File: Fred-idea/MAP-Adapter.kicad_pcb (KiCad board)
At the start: 2 copper layers, 19.8 x 11.5 mm, 2 parts, among them U1 SOP8, U6 SSOP8

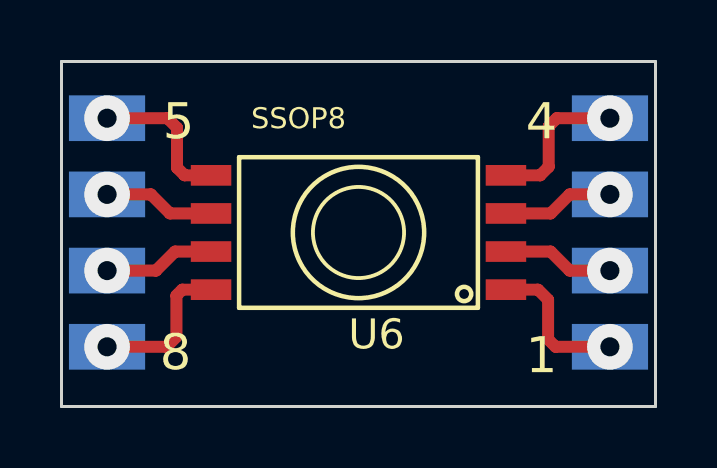
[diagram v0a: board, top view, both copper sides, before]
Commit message: Widened traces on top (SSOP) layer to the same width as the SSOP pads.
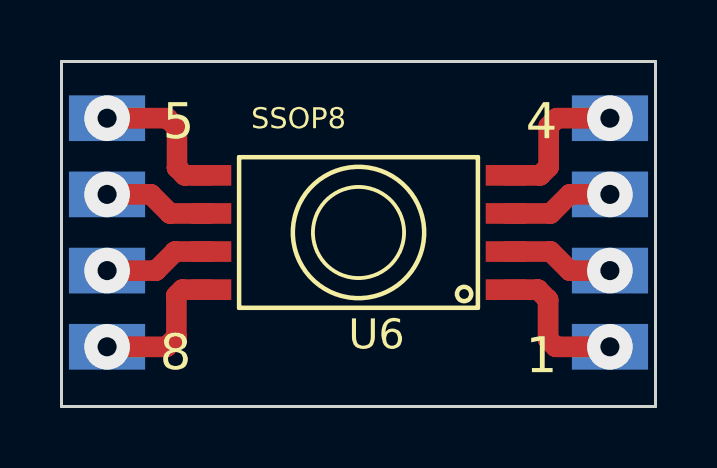
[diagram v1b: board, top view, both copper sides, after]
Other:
- net class SSOP: trace_width 0.4 -> 0.69
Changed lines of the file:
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@@
   (net_class SSOP ""
     (clearance 0.254)
-    (trace_width 0.4)
+    (trace_width 0.69)
     (via_dia 1.524)
     (via_drill 1.2)
@@
   (gr_line (start 226.3 144.8) (end 206.5 144.8) (angle 90) (layer Edge.Cuts) (width 0.1))
   (gr_line (start 226.3 156.3) (end 226.3 144.8) (angle 90) (layer Edge.Cuts) (width 0.1))
-  (segment (start 221.315 151.135) (end 222.805 151.135) (width 0.4) (layer F.Cu) (net 1))
-  (segment (start 224.78 151.77) (end 224.782 151.77) (width 0.4) (layer B.Cu) (net 1))
+  (segment (start 221.315 151.135) (end 222.805 151.135) (width 0.69) (layer F.Cu) (net 1))
+  (segment (start 222.805 151.135) (end 223.44 151.77) (width 0.69) (layer F.Cu) (net 1))
+  (segment (start 223.44 151.77) (end 224.78 151.77) (width 0.69) (layer F.Cu) (net 1))
   (via (at 224.78 151.77) (size 1.524) (layers F.Cu B.Cu) (net 1))
-  (segment (start 223.44 151.77) (end 224.78 151.77) (width 0.4) (layer F.Cu) (net 1))
-  (segment (start 222.805 151.135) (end 223.44 151.77) (width 0.4) (layer F.Cu) (net 1))
-  (segment (start 221.315 149.865) (end 222.805 149.865) (width 0.4) (layer F.Cu) (net 2))
-  (segment (start 224.78 149.23) (end 224.782 149.23) (width 0.4) (layer B.Cu) (net 2))
+  (segment (start 224.78 151.77) (end 224.782 151.77) (width 0.69) (layer B.Cu) (net 1))
+  (segment (start 221.315 149.865) (end 222.805 149.865) (width 0.69) (layer F.Cu) (net 2))
+  (segment (start 222.805 149.865) (end 223.44 149.23) (width 0.69) (layer F.Cu) (net 2))
+  (segment (start 223.44 149.23) (end 224.78 149.23) (width 0.69) (layer F.Cu) (net 2))
   (via (at 224.78 149.23) (size 1.524) (layers F.Cu B.Cu) (net 2))
-  (segment (start 223.44 149.23) (end 224.78 149.23) (width 0.4) (layer F.Cu) (net 2))
-  (segment (start 222.805 149.865) (end 223.44 149.23) (width 0.4) (layer F.Cu) (net 2))
-  (segment (start 221.315 148.595) (end 222.455 148.595) (width 0.4) (layer F.Cu) (net 3))
-  (segment (start 224.78 146.69) (end 224.782 146.69) (width 0.4) (layer B.Cu) (net 3))
+  (segment (start 224.78 149.23) (end 224.782 149.23) (width 0.69) (layer B.Cu) (net 2))
+  (segment (start 221.315 148.595) (end 222.455 148.595) (width 0.69) (layer F.Cu) (net 3))
+  (segment (start 222.455 148.595) (end 222.74 148.31) (width 0.69) (layer F.Cu) (net 3))
+  (segment (start 222.74 148.31) (end 222.74 146.96) (width 0.69) (layer F.Cu) (net 3))
+  (segment (start 222.74 146.96) (end 223.01 146.69) (width 0.69) (layer F.Cu) (net 3))
+  (segment (start 223.01 146.69) (end 224.78 146.69) (width 0.69) (layer F.Cu) (net 3))
   (via (at 224.78 146.69) (size 1.524) (layers F.Cu B.Cu) (net 3))
-  (segment (start 223.01 146.69) (end 224.78 146.69) (width 0.4) (layer F.Cu) (net 3))
-  (segment (start 222.74 146.96) (end 223.01 146.69) (width 0.4) (layer F.Cu) (net 3))
-  (segment (start 222.74 148.31) (end 222.74 146.96) (width 0.4) (layer F.Cu) (net 3))
-  (segment (start 222.455 148.595) (end 222.74 148.31) (width 0.4) (layer F.Cu) (net 3))
-  (segment (start 221.315 152.405) (end 222.385 152.405) (width 0.4) (layer F.Cu) (net 4))
-  (segment (start 224.78 154.31) (end 224.782 154.31) (width 0.4) (layer B.Cu) (net 4))
+  (segment (start 224.78 146.69) (end 224.782 146.69) (width 0.69) (layer B.Cu) (net 3))
+  (segment (start 221.315 152.405) (end 222.385 152.405) (width 0.69) (layer F.Cu) (net 4))
+  (segment (start 222.385 152.405) (end 222.72 152.74) (width 0.69) (layer F.Cu) (net 4))
+  (segment (start 222.72 152.74) (end 222.72 154.06) (width 0.69) (layer F.Cu) (net 4))
+  (segment (start 222.72 154.06) (end 222.97 154.31) (width 0.69) (layer F.Cu) (net 4))
+  (segment (start 222.97 154.31) (end 224.78 154.31) (width 0.69) (layer F.Cu) (net 4))
   (via (at 224.78 154.31) (size 1.524) (layers F.Cu B.Cu) (net 4))
-  (segment (start 222.97 154.31) (end 224.78 154.31) (width 0.4) (layer F.Cu) (net 4))
-  (segment (start 222.72 154.06) (end 222.97 154.31) (width 0.4) (layer F.Cu) (net 4))
-  (segment (start 222.72 152.74) (end 222.72 154.06) (width 0.4) (layer F.Cu) (net 4))
-  (segment (start 222.385 152.405) (end 222.72 152.74) (width 0.4) (layer F.Cu) (net 4))
-  (segment (start 211.485 148.595) (end 210.605 148.595) (width 0.4) (layer F.Cu) (net 5))
-  (segment (start 208.02 146.69) (end 208.018 146.69) (width 0.4) (layer B.Cu) (net 5))
+  (segment (start 224.78 154.31) (end 224.782 154.31) (width 0.69) (layer B.Cu) (net 4))
+  (segment (start 211.485 148.595) (end 210.605 148.595) (width 0.69) (layer F.Cu) (net 5))
+  (segment (start 210.605 148.595) (end 210.35 148.34) (width 0.69) (layer F.Cu) (net 5))
+  (segment (start 210.35 148.34) (end 210.35 147.01) (width 0.69) (layer F.Cu) (net 5))
+  (segment (start 210.35 147.01) (end 210.03 146.69) (width 0.69) (layer F.Cu) (net 5))
+  (segment (start 210.03 146.69) (end 208.02 146.69) (width 0.69) (layer F.Cu) (net 5))
   (via (at 208.02 146.69) (size 1.524) (layers F.Cu B.Cu) (net 5))
-  (segment (start 210.03 146.69) (end 208.02 146.69) (width 0.4) (layer F.Cu) (net 5))
-  (segment (start 210.35 147.01) (end 210.03 146.69) (width 0.4) (layer F.Cu) (net 5))
-  (segment (start 210.35 148.34) (end 210.35 147.01) (width 0.4) (layer F.Cu) (net 5))
-  (segment (start 210.605 148.595) (end 210.35 148.34) (width 0.4) (layer F.Cu) (net 5))
-  (segment (start 211.485 149.865) (end 210.115 149.865) (width 0.4) (layer F.Cu) (net 6))
-  (segment (start 208.02 149.23) (end 208.018 149.23) (width 0.4) (layer B.Cu) (net 6))
+  (segment (start 208.02 146.69) (end 208.018 146.69) (width 0.69) (layer B.Cu) (net 5))
+  (segment (start 211.485 149.865) (end 210.115 149.865) (width 0.69) (layer F.Cu) (net 6))
+  (segment (start 210.115 149.865) (end 209.48 149.23) (width 0.69) (layer F.Cu) (net 6))
+  (segment (start 209.48 149.23) (end 208.02 149.23) (width 0.69) (layer F.Cu) (net 6))
   (via (at 208.02 149.23) (size 1.524) (layers F.Cu B.Cu) (net 6))
-  (segment (start 209.48 149.23) (end 208.02 149.23) (width 0.4) (layer F.Cu) (net 6))
-  (segment (start 210.115 149.865) (end 209.48 149.23) (width 0.4) (layer F.Cu) (net 6))
-  (segment (start 211.485 151.135) (end 210.285 151.135) (width 0.4) (layer F.Cu) (net 7))
-  (segment (start 208.02 151.77) (end 208.018 151.77) (width 0.4) (layer B.Cu) (net 7))
+  (segment (start 208.02 149.23) (end 208.018 149.23) (width 0.69) (layer B.Cu) (net 6))
+  (segment (start 211.485 151.135) (end 210.285 151.135) (width 0.69) (layer F.Cu) (net 7))
+  (segment (start 210.285 151.135) (end 209.65 151.77) (width 0.69) (layer F.Cu) (net 7))
+  (segment (start 209.65 151.77) (end 208.02 151.77) (width 0.69) (layer F.Cu) (net 7))
   (via (at 208.02 151.77) (size 1.524) (layers F.Cu B.Cu) (net 7))
-  (segment (start 209.65 151.77) (end 208.02 151.77) (width 0.4) (layer F.Cu) (net 7))
-  (segment (start 210.285 151.135) (end 209.65 151.77) (width 0.4) (layer F.Cu) (net 7))
-  (segment (start 211.485 152.405) (end 210.525 152.405) (width 0.4) (layer F.Cu) (net 8))
-  (segment (start 208.02 154.31) (end 208.018 154.31) (width 0.4) (layer B.Cu) (net 8))
+  (segment (start 208.02 151.77) (end 208.018 151.77) (width 0.69) (layer B.Cu) (net 7))
+  (segment (start 211.485 152.405) (end 210.525 152.405) (width 0.69) (layer F.Cu) (net 8))
+  (segment (start 210.525 152.405) (end 210.33 152.6) (width 0.69) (layer F.Cu) (net 8))
+  (segment (start 210.33 152.6) (end 210.33 153.98) (width 0.69) (layer F.Cu) (net 8))
+  (segment (start 210.33 153.98) (end 210 154.31) (width 0.69) (layer F.Cu) (net 8))
+  (segment (start 210 154.31) (end 208.02 154.31) (width 0.69) (layer F.Cu) (net 8))
   (via (at 208.02 154.31) (size 1.524) (layers F.Cu B.Cu) (net 8))
-  (segment (start 210 154.31) (end 208.02 154.31) (width 0.4) (layer F.Cu) (net 8))
-  (segment (start 210.33 153.98) (end 210 154.31) (width 0.4) (layer F.Cu) (net 8))
-  (segment (start 210.33 152.6) (end 210.33 153.98) (width 0.4) (layer F.Cu) (net 8))
-  (segment (start 210.525 152.405) (end 210.33 152.6) (width 0.4) (layer F.Cu) (net 8))
+  (segment (start 208.02 154.31) (end 208.018 154.31) (width 0.69) (layer B.Cu) (net 8))
 )

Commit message: Edges of PCB are now at the edge of the solder mask.
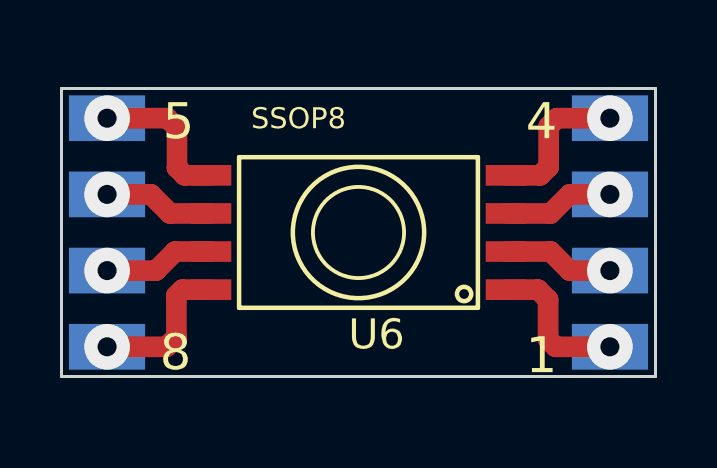
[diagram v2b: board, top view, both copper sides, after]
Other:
- board size 19.8 x 11.5 mm -> 19.8 x 9.6 mm
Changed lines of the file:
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@@
     )
   )
+  (dimension 9.6 (width 0.3) (layer Eco1.User)
+    (gr_text "0.3780 in" (at 230.95 150.5 90) (layer Eco1.User)
+      (effects (font (size 1.5 1.5) (thickness 0.3)))
+    )
+    (feature1 (pts (xy 226.6 145.7) (xy 232.3 145.7)))
+    (feature2 (pts (xy 226.6 155.3) (xy 232.3 155.3)))
+    (crossbar (pts (xy 229.6 155.3) (xy 229.6 145.7)))
+    (arrow1a (pts (xy 229.6 145.7) (xy 230.18642 146.826503)))
+    (arrow1b (pts (xy 229.6 145.7) (xy 229.01358 146.826503)))
+    (arrow2a (pts (xy 229.6 155.3) (xy 230.18642 154.173497)))
+    (arrow2b (pts (xy 229.6 155.3) (xy 229.01358 154.173497)))
+  )
+  (dimension 19.8 (width 0.3) (layer Eco1.User)
+    (gr_text "0.7795 in" (at 216.4 142.950001) (layer Eco1.User)
+      (effects (font (size 1.5 1.5) (thickness 0.3)))
+    )
+    (feature1 (pts (xy 226.3 145.4) (xy 226.3 141.600001)))
+    (feature2 (pts (xy 206.5 145.4) (xy 206.5 141.600001)))
+    (crossbar (pts (xy 206.5 144.300001) (xy 226.3 144.300001)))
+    (arrow1a (pts (xy 226.3 144.300001) (xy 225.173497 144.886421)))
+    (arrow1b (pts (xy 226.3 144.300001) (xy 225.173497 143.713581)))
+    (arrow2a (pts (xy 206.5 144.300001) (xy 207.626503 144.886421)))
+    (arrow2b (pts (xy 206.5 144.300001) (xy 207.626503 143.713581)))
+  )
+  (dimension 9.6 (width 0.3) (layer Dwgs.User)
+    (gr_text "9.600 mm" (at 203.55 150.5 90) (layer Dwgs.User)
+      (effects (font (size 1.5 1.5) (thickness 0.3)))
+    )
+    (feature1 (pts (xy 206.2 145.7) (xy 202.2 145.7)))
+    (feature2 (pts (xy 206.2 155.3) (xy 202.2 155.3)))
+    (crossbar (pts (xy 204.9 155.3) (xy 204.9 145.7)))
+    (arrow1a (pts (xy 204.9 145.7) (xy 205.48642 146.826503)))
+    (arrow1b (pts (xy 204.9 145.7) (xy 204.31358 146.826503)))
+    (arrow2a (pts (xy 204.9 155.3) (xy 205.48642 154.173497)))
+    (arrow2b (pts (xy 204.9 155.3) (xy 204.31358 154.173497)))
+  )
+  (dimension 19.8 (width 0.3) (layer Dwgs.User)
+    (gr_text "19.800 mm" (at 216.4 158.349999) (layer Dwgs.User)
+      (effects (font (size 1.5 1.5) (thickness 0.3)))
+    )
+    (feature1 (pts (xy 226.3 155.6) (xy 226.3 159.699999)))
+    (feature2 (pts (xy 206.5 155.6) (xy 206.5 159.699999)))
+    (crossbar (pts (xy 206.5 156.999999) (xy 226.3 156.999999)))
+    (arrow1a (pts (xy 226.3 156.999999) (xy 225.173497 157.586419)))
+    (arrow1b (pts (xy 226.3 156.999999) (xy 225.173497 156.413579)))
+    (arrow2a (pts (xy 206.5 156.999999) (xy 207.626503 157.586419)))
+    (arrow2b (pts (xy 206.5 156.999999) (xy 207.626503 156.413579)))
+  )
+  (gr_line (start 206.5 155.3) (end 206.5 145.7) (angle 90) (layer Edge.Cuts) (width 0.1))
+  (gr_line (start 226.3 155.3) (end 206.5 155.3) (angle 90) (layer Edge.Cuts) (width 0.1))
+  (gr_line (start 226.3 145.7) (end 226.3 155.3) (angle 90) (layer Edge.Cuts) (width 0.1))
+  (gr_line (start 206.5 145.7) (end 226.3 145.7) (angle 90) (layer Edge.Cuts) (width 0.1))
   (gr_text 8 (at 210.3 154.5) (layer F.SilkS)
     (effects (font (size 1.2 1.2) (thickness 0.18)))
@@
     (effects (font (size 1.2 1.2) (thickness 0.18)))
   )
-  (dimension 19.8 (width 0.3) (layer Dwgs.User)
-    (gr_text "19.800 mm" (at 216.4 159.249999) (layer Dwgs.User)
-      (effects (font (size 1.5 1.5) (thickness 0.3)))
-    )
-    (feature1 (pts (xy 226.3 156.6) (xy 226.3 160.599999)))
-    (feature2 (pts (xy 206.5 156.6) (xy 206.5 160.599999)))
-    (crossbar (pts (xy 206.5 157.899999) (xy 226.3 157.899999)))
-    (arrow1a (pts (xy 226.3 157.899999) (xy 225.173497 158.486419)))
-    (arrow1b (pts (xy 226.3 157.899999) (xy 225.173497 157.313579)))
-    (arrow2a (pts (xy 206.5 157.899999) (xy 207.626503 158.486419)))
-    (arrow2b (pts (xy 206.5 157.899999) (xy 207.626503 157.313579)))
-  )
-  (dimension 11.5 (width 0.3) (layer Dwgs.User)
-    (gr_text "11.500 mm" (at 203.75 150.55 90) (layer Dwgs.User)
-      (effects (font (size 1.5 1.5) (thickness 0.3)))
-    )
-    (feature1 (pts (xy 206.3 144.8) (xy 202.4 144.8)))
-    (feature2 (pts (xy 206.3 156.3) (xy 202.4 156.3)))
-    (crossbar (pts (xy 205.1 156.3) (xy 205.1 144.8)))
-    (arrow1a (pts (xy 205.1 144.8) (xy 205.68642 145.926503)))
-    (arrow1b (pts (xy 205.1 144.8) (xy 204.51358 145.926503)))
-    (arrow2a (pts (xy 205.1 156.3) (xy 205.68642 155.173497)))
-    (arrow2b (pts (xy 205.1 156.3) (xy 204.51358 155.173497)))
-  )
-  (dimension 11.5 (width 0.3) (layer Eco1.User)
-    (gr_text "0.4528 in" (at 229.15 150.55 90) (layer Eco1.User)
-      (effects (font (size 1.5 1.5) (thickness 0.3)))
-    )
-    (feature1 (pts (xy 226.6 144.8) (xy 230.5 144.8)))
-    (feature2 (pts (xy 226.6 156.3) (xy 230.5 156.3)))
-    (crossbar (pts (xy 227.8 156.3) (xy 227.8 144.8)))
-    (arrow1a (pts (xy 227.8 144.8) (xy 228.38642 145.926503)))
-    (arrow1b (pts (xy 227.8 144.8) (xy 227.21358 145.926503)))
-    (arrow2a (pts (xy 227.8 156.3) (xy 228.38642 155.173497)))
-    (arrow2b (pts (xy 227.8 156.3) (xy 227.21358 155.173497)))
-  )
-  (dimension 19.8 (width 0.3) (layer Eco1.User)
-    (gr_text "0.7795 in" (at 216.4 142.150001) (layer Eco1.User)
-      (effects (font (size 1.5 1.5) (thickness 0.3)))
-    )
-    (feature1 (pts (xy 226.3 144.5) (xy 226.3 140.800001)))
-    (feature2 (pts (xy 206.5 144.5) (xy 206.5 140.800001)))
-    (crossbar (pts (xy 206.5 143.500001) (xy 226.3 143.500001)))
-    (arrow1a (pts (xy 226.3 143.500001) (xy 225.173497 144.086421)))
-    (arrow1b (pts (xy 226.3 143.500001) (xy 225.173497 142.913581)))
-    (arrow2a (pts (xy 206.5 143.500001) (xy 207.626503 144.086421)))
-    (arrow2b (pts (xy 206.5 143.500001) (xy 207.626503 142.913581)))
-  )
-  (gr_line (start 206.5 156.3) (end 226.3 156.3) (angle 90) (layer Edge.Cuts) (width 0.1))
-  (gr_line (start 206.5 144.8) (end 206.5 156.3) (angle 90) (layer Edge.Cuts) (width 0.1))
-  (gr_line (start 226.3 144.8) (end 206.5 144.8) (angle 90) (layer Edge.Cuts) (width 0.1))
-  (gr_line (start 226.3 156.3) (end 226.3 144.8) (angle 90) (layer Edge.Cuts) (width 0.1))
   (segment (start 221.315 151.135) (end 222.805 151.135) (width 0.69) (layer F.Cu) (net 1))
   (segment (start 222.805 151.135) (end 223.44 151.77) (width 0.69) (layer F.Cu) (net 1))
